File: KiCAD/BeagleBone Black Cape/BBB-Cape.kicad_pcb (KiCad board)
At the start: 2 copper layers, 54.6 x 86.4 mm, 85 parts, among them J1 MOUNTING_HOLE, J10 Conn_01x02, J11 RJ45-TRANSFO, J12 DB9_Female, J2 MOUNTING_HOLE, J3 MOUNTING_HOLE, J4 MOUNTING_HOLE, J5 MOUNTING_HOLE, J6 MOUNTING_HOLE, J7 MOUNTING_HOLE, J8 MOUNTING_HOLE, J9 01x06_Stackable Header, P1 02x23_Stackable Header, P2 02x23_Stackable Header, SW1 W5500_RST, SW2 SYS_RST, SW3 Power, U1 LM25576MH, U2 WIZnet W5500, U3 MAX13433EETD, Y1 25MHz

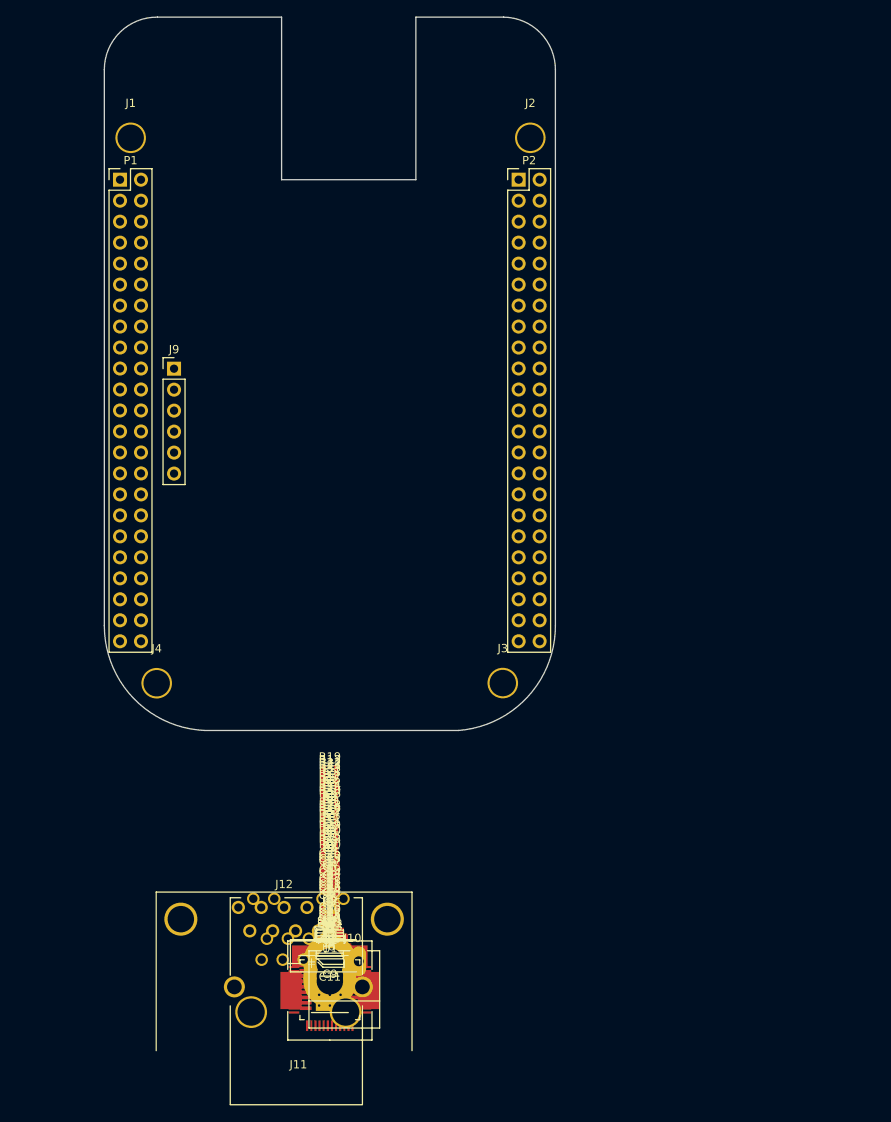
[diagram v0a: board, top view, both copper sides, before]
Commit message: BeagleBone Updated, headers need to be moved into proper spot
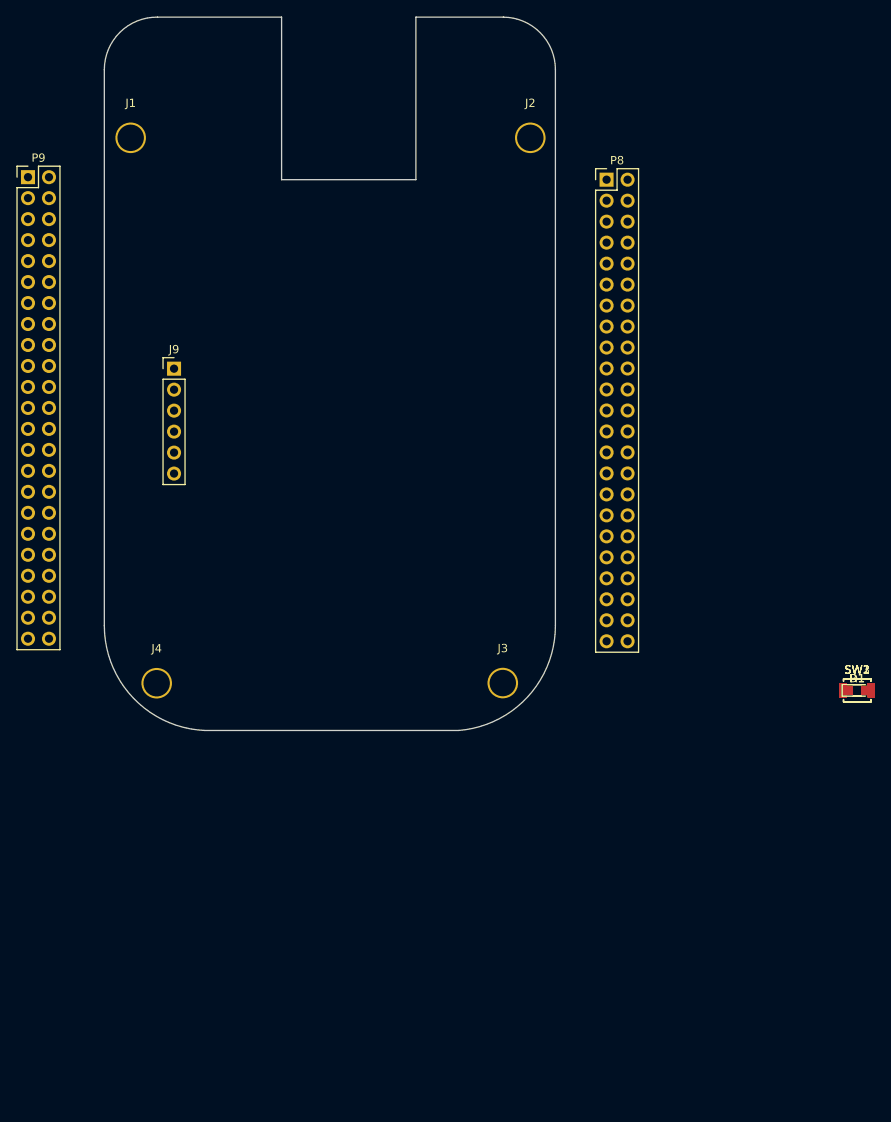
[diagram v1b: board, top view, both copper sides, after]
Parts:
- removed C1: 1.00uF, Capacitors_SMD:C_0603
- removed C10, C12, C13, C14, C15, C18, C19, C2, C26, C27: 0.1uF, Capacitors_SMD:C_0603
- removed C11, C9: 10uF, Capacitors_SMD:CP_Elec_3x5.3
- removed C16, C17: 6.8nF, Capacitors_SMD:C_0603
- removed C20, C23: 10nF, Capacitors_SMD:C_0603
- removed C21, C5: 22nF, Capacitors_SMD:C_0603
- removed C22: 4.7uF, Capacitors_SMD:C_0603
- removed C24, C25: 18pF, Capacitors_SMD:C_0603
- removed C3: 270pF, Capacitors_SMD:C_0603
- removed C4: 1.80nF, Capacitors_SMD:C_0603
- removed C6: 8.2nF, Capacitors_SMD:C_0603
- removed C7, C8: 47uF, Capacitors_SMD:C_0603
- removed D2: 0.455V 20.0A, Diodes_SMD:D_0805
- removed J10: Conn_01x02, Connectors_Phoenix:PhoenixContact_MC-G_02x3.50mm_Angled
- removed J11: RJ45-TRANSFO, Connectors:RJ45_TRANSFO
- removed J12: DB9_Female, Connectors_DSub:DSUB-9_Female_Horizontal_Pitch2.77x2.84mm_EdgePinOffset14.56mm_Housed_MountingHolesOffset15.98mm
- removed J5, J6, J7, J8: MOUNTING_HOLE, Mounting_Holes:MountingHole_3.2mm_M3_Pad
- removed L1: 27.0uH, Inductors_SMD:L_Wuerth_HCM-1240
- removed L2: BLM21PG121SN1D, Inductors_SMD:L_0805_HandSoldering
- removed P1, P2: 02x23_Stackable Header, Pin_Headers:Pin_Header_Straight_2x23_Pitch2.54mm
- removed R10, R11: 82, Resistors_SMD:R_0603
- removed R12: 10, Resistors_SMD:R_0603
- removed R13: 12.4k, Resistors_SMD:R_0603
- removed R14, R15, R16, R17, R18, R19, R20, R21, R22, R23, R24: 10k, Resistors_SMD:R_0603
- removed R2: 16.2k, Resistors_SMD:R_0603
- removed R25: 10M, Resistors_SMD:R_0603
- removed R26, R27: 20k, Resistors_SMD:R_0603
- removed R28, R29, R30, R31: 0, Resistors_SMD:R_0603
- removed R3: 22.1k, Resistors_SMD:R_0603
- removed R32, R33: 120, Resistors_SMD:R_0603
- removed R4: 3.09k, Resistors_SMD:R_0603
- removed R5: 1.02k, Resistors_SMD:R_0603
- removed R6, R9: 49.9, Resistors_SMD:R_0603
- removed R7, R8: 330, Resistors_SMD:R_0603
- removed U1: LM25576MH, Housings_SSOP:HTSSOP-20-1EP_4.4x6.5mm_Pitch0.65mm_ThermalPad
- removed U2: WIZnet W5500, Housings_QFP:LQFP-48_7x7mm_Pitch0.5mm
- removed U3: MAX13433EETD, Housings_DFN_QFN:DFN-14-1EP_3x4mm_Pitch0.5mm
- removed Y1: 25MHz, Crystals:Crystal_SMD_0603-2pin_6.0x3.5mm_HandSoldering
- added P8: 02x23_Stackable Header, Pin_Headers:Pin_Header_Straight_2x23_Pitch2.54mm, F.Cu at (171.5, 67.2)
- added P9: 02x23_Stackable Header, Pin_Headers:Pin_Header_Straight_2x23_Pitch2.54mm, F.Cu at (101.4, 66.9)
- moved SW3 71.0 mm to (201.8, 129.0)
- moved SW2 70.9 mm to (201.8, 129.0)
- moved SW1 70.7 mm to (201.8, 129.0)
- moved D1 70.3 mm to (201.8, 129.0)
- moved R1 66.0 mm to (201.8, 129.0)
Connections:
- J9 pad 1: DGND -> (no net)
- SW1 pad 1: W5500_RST -> (no net)
